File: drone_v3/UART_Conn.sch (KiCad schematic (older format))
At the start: 14 parts, among them J15 UART4_con, J3 UART4_con, J4 Conn_01x04_Male, J5 Conn_01x02_Female, J6 Conn_01x04_Male, J7 Conn_01x04_Male, J8 UART4_con, J9 Conn_01x06_Male, Q1 2N3904

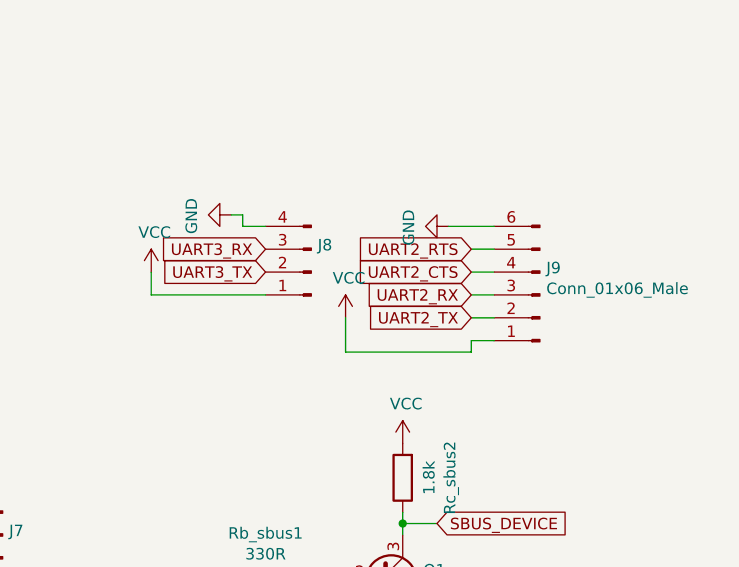
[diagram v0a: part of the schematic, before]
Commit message: cystal layout
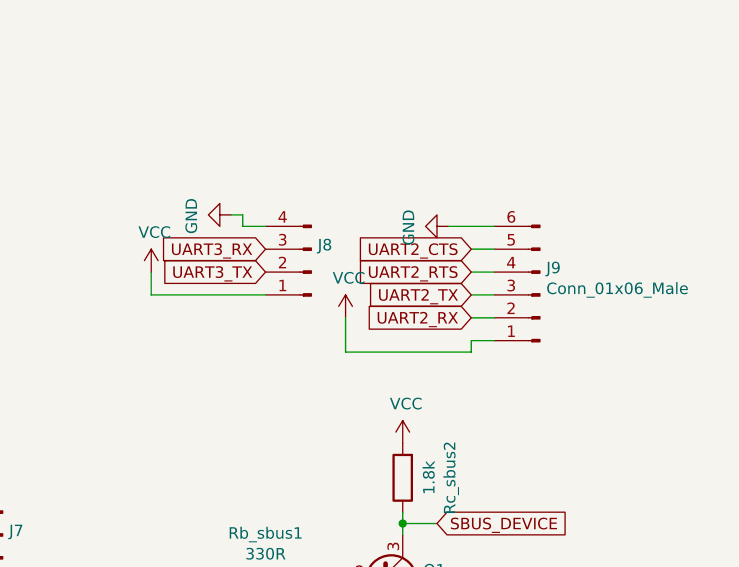
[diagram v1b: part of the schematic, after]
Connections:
- net UART2_CTS: now also J9.5 (Pin_5); no longer J9.4 (Pin_4)
- net UART2_RTS: now also J9.4 (Pin_4); no longer J9.5 (Pin_5)
- net UART2_RX: now also J9.2 (Pin_2); no longer J9.3 (Pin_3)
- net UART2_TX: now also J9.3 (Pin_3); no longer J9.2 (Pin_2)
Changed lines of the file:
@@
 	0    1    1    0
 $EndComp
+Text GLabel 7950 3250 0    50   Input ~ 0
+UART2_TX
 Text GLabel 7950 3350 0    50   Input ~ 0
-UART2_TX
-Text GLabel 7950 3250 0    50   Input ~ 0
 UART2_RX
 $Comp
@@
 	7850 2950 8050 2950
 Wire Wire Line
+	7950 3150 8050 3150
+Wire Wire Line
 	7950 3050 8050 3050
-Wire Wire Line
-	7950 3150 8050 3150
 $Comp
 L Connector:Conn_01x04_Male J?
@@
 Wire Wire Line
 	8050 3450 7950 3450
+Text GLabel 7950 3050 0    50   Input ~ 0
+UART2_CTS
 Text GLabel 7950 3150 0    50   Input ~ 0
-UART2_CTS
-Text GLabel 7950 3050 0    50   Input ~ 0
 UART2_RTS
 Wire Wire Line
+	7950 3250 8050 3250
+Wire Wire Line
 	7950 3350 8050 3350
-Wire Wire Line
-	7950 3250 8050 3250
-$Comp
-L Connector:Conn_01x04_Male J?
+$Comp
+L Connector:Conn_01x04_Male J?
